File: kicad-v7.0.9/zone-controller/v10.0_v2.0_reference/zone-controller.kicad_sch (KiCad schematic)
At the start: 48 parts, among them J15 EBBA-02-C-SS-BU, P1 1x3_pin_header, P2 1x3_pin_header, P3 1x3_pin_header, P4 1x3_pin_header, P5 1x3_pin_header, P6 1x3_pin_header, Q13 PMV213SN,215, Q14 PMV213SN,215, SW13 SMTS-102-2C2T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

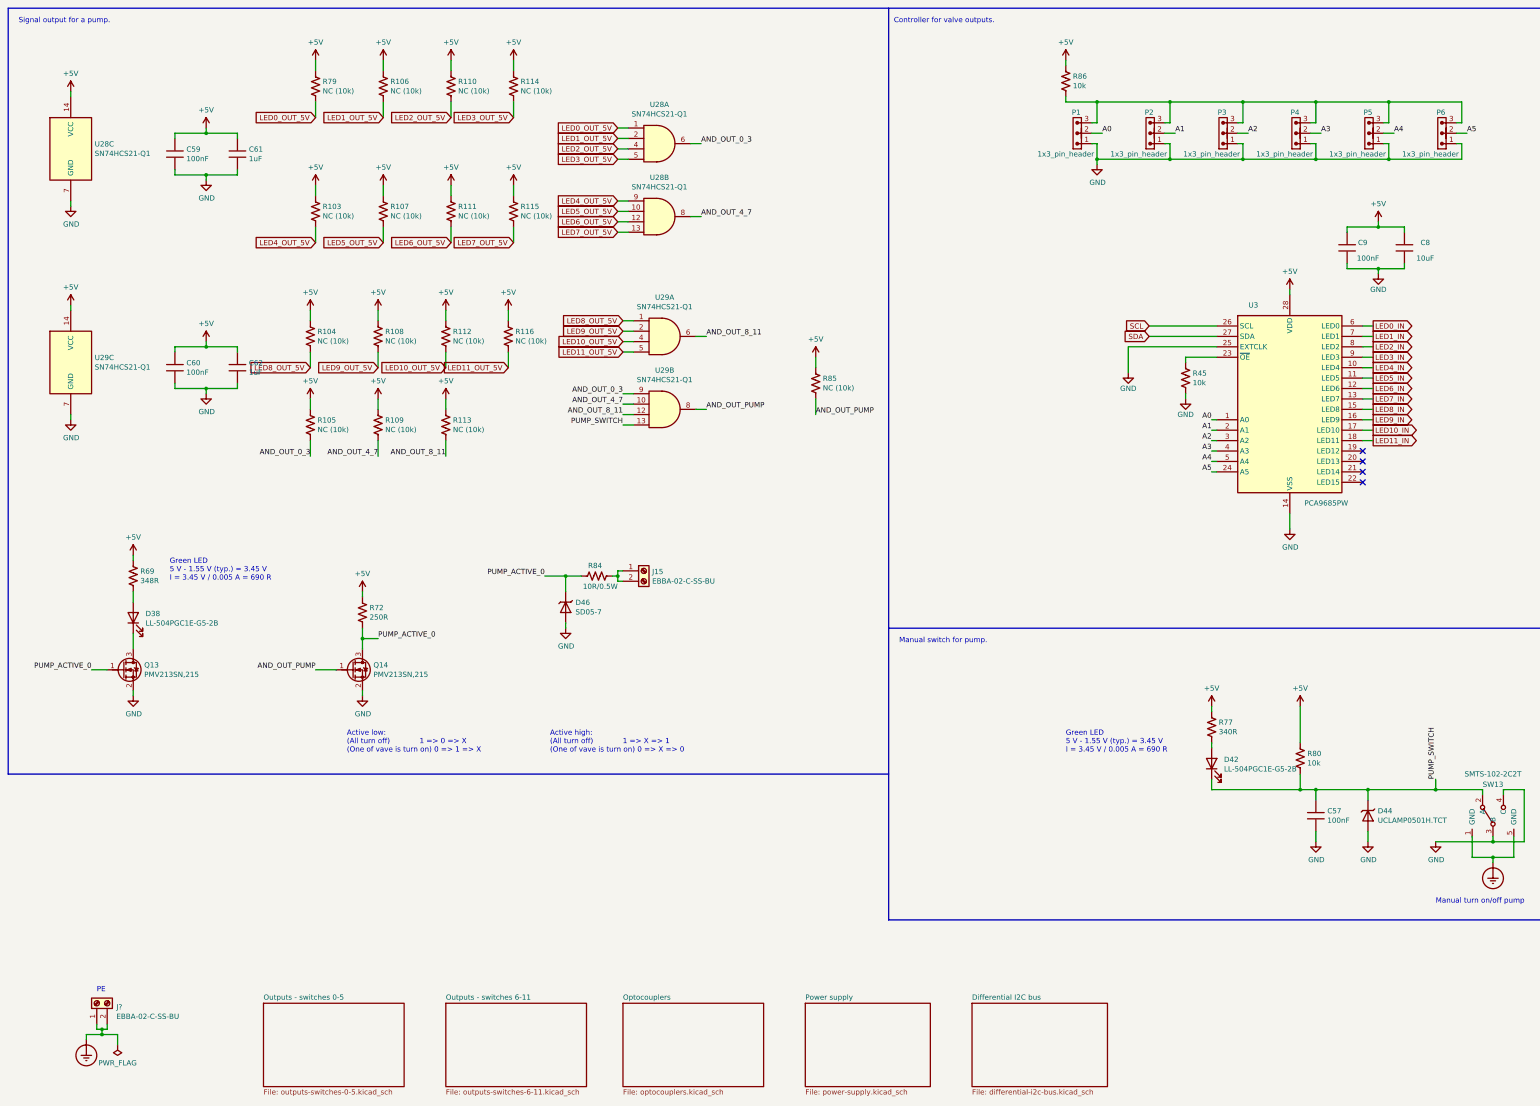
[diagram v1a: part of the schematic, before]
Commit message: Zone controller. Change library. Small changes in schematic a PCB.
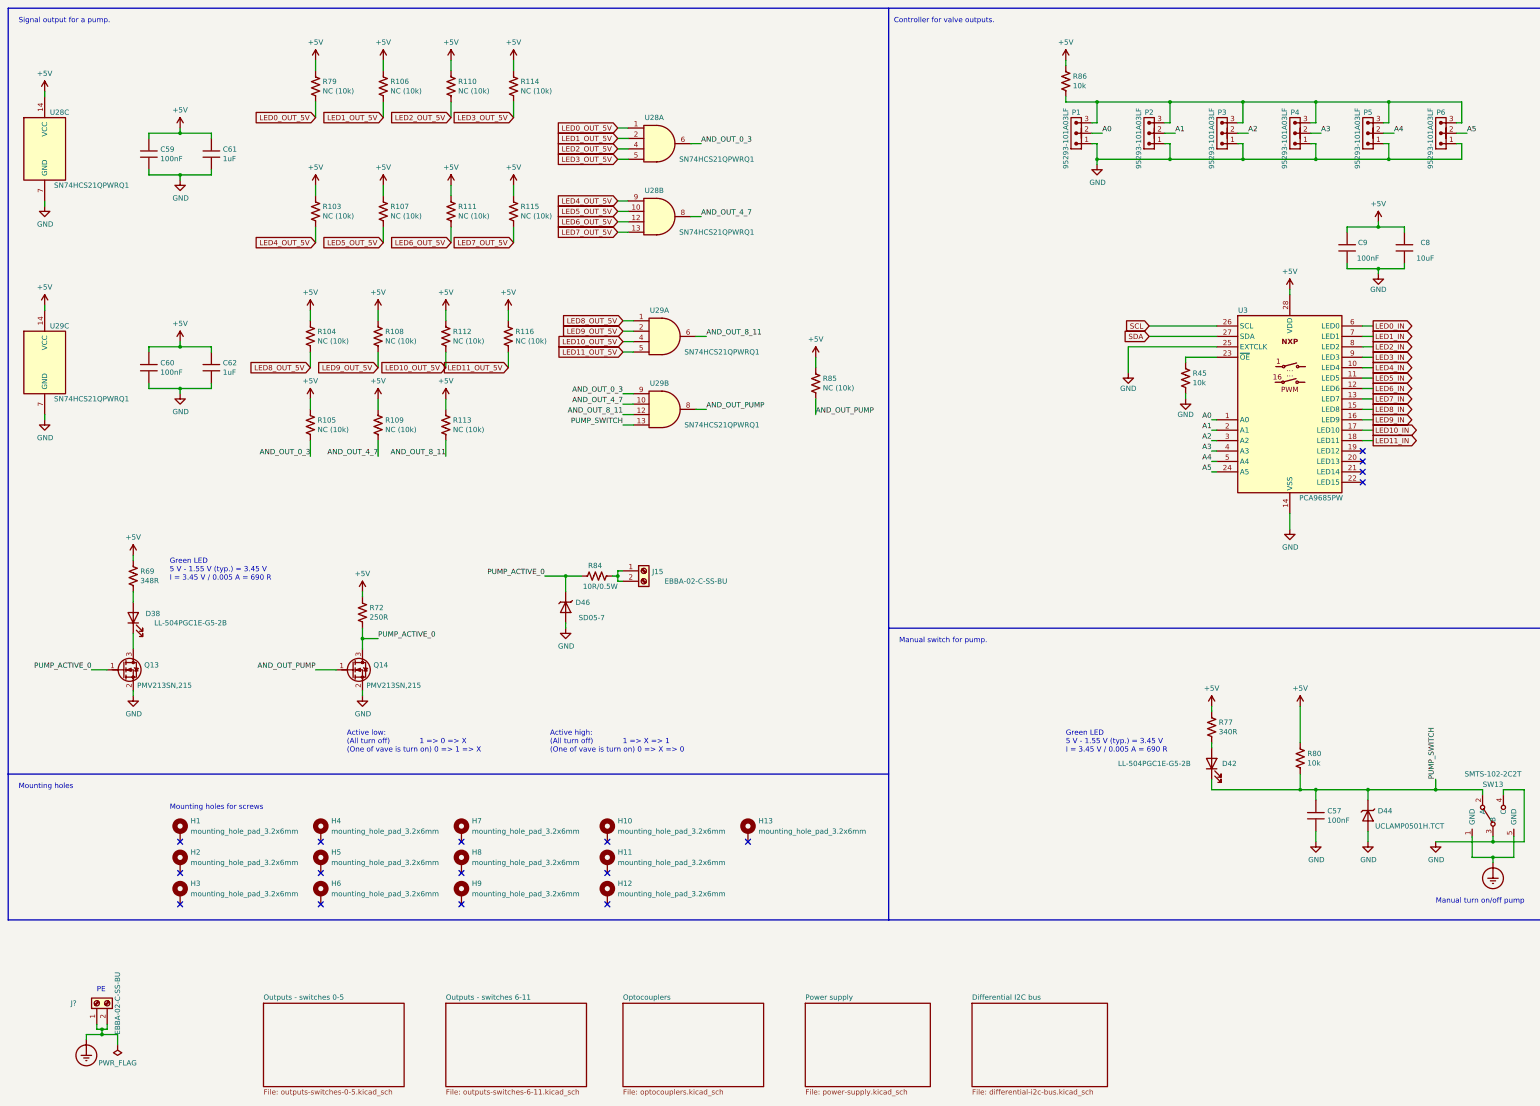
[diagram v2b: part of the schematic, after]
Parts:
- added H1, H10, H11, H12, H13, H2, H3, H4, H5, H6, H7, H8, H9: mounting_hole_pad_3.2x6mm, mounting_hole_pad_rl:mounting_hole_pad_3.2x6mm, symbol mounting_hole_pad_rl:mounting_hole_pad_3.2x6mm
- C57, C59, C60, C61, C62, C8, C9: symbol passive_component_rl:capacitor -> capacitor_smd_rl:c_1206
- D38, D42: symbol diode_rl:LED -> led_tht_rl:LL-504PGC1E-G5-2B
- D44: symbol diode_rl:undir_transil -> transil_diode_smd_rl:UCLAMP0501H.TCT
- D46: symbol diode_rl:undir_transil -> transil_diode_smd_rl:SD05-7
- J15, J?: symbol connector_rl:1x2_screw_term_block -> terminal_block_tht_rl:EBBA-02-C-SS-BU
- P1, P2, P3, P4, P5, P6: value 1x3_pin_header -> 95293-101A03LF; symbol connector_rl:1x3_pin_header -> connector_smd_pin_header_2.54mm_rl:95293-101A03LF
- Q13, Q14: symbol unipolar_transistor_rl:n_mosfet_gsd -> unipolar_transistor_smd_rl:PMV213SN,215
- R103, R104, R105, R106, R107, R108, R109, R110, R111, R112, R113, R114, R115, R116, R45, R69, R72, R77, R79, R80, R84, R85, R86: symbol passive_component_rl:resistor_us -> resistor_smd_rl:r_1206_us
- SW13: symbol switch_rl:SMTS-102-2C2T -> switch_tht_rl:SMTS-102-2C2T
- U28, U29: value SN74HCS21-Q1 -> SN74HCS21QPWRQ1; symbol 74xx_rl:SN74HCS21-Q1 -> 74xx_rl:SN74HCS21QPWRQ1
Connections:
- no-connect marks 4 -> 17
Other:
- note added: "Mounting holes"
- note added: "Mounting holes for screws"
- moved on the sheet: C59, C60, C61, C62, U28C, U29C
